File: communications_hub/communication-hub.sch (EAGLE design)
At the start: 47 parts, among them CON1 SM04B-GHS-TB, CON2 SM04B-GHS-TB, CON3 SM02B-GHS-TB, CON4 SM04B-GHS-TB, CON5 SM04B-GHS-TB, Q1 DMN5L06K, Q2 DMN5L06K, U1 TCAN1042HVDR, U2 TCAN1042HVDR

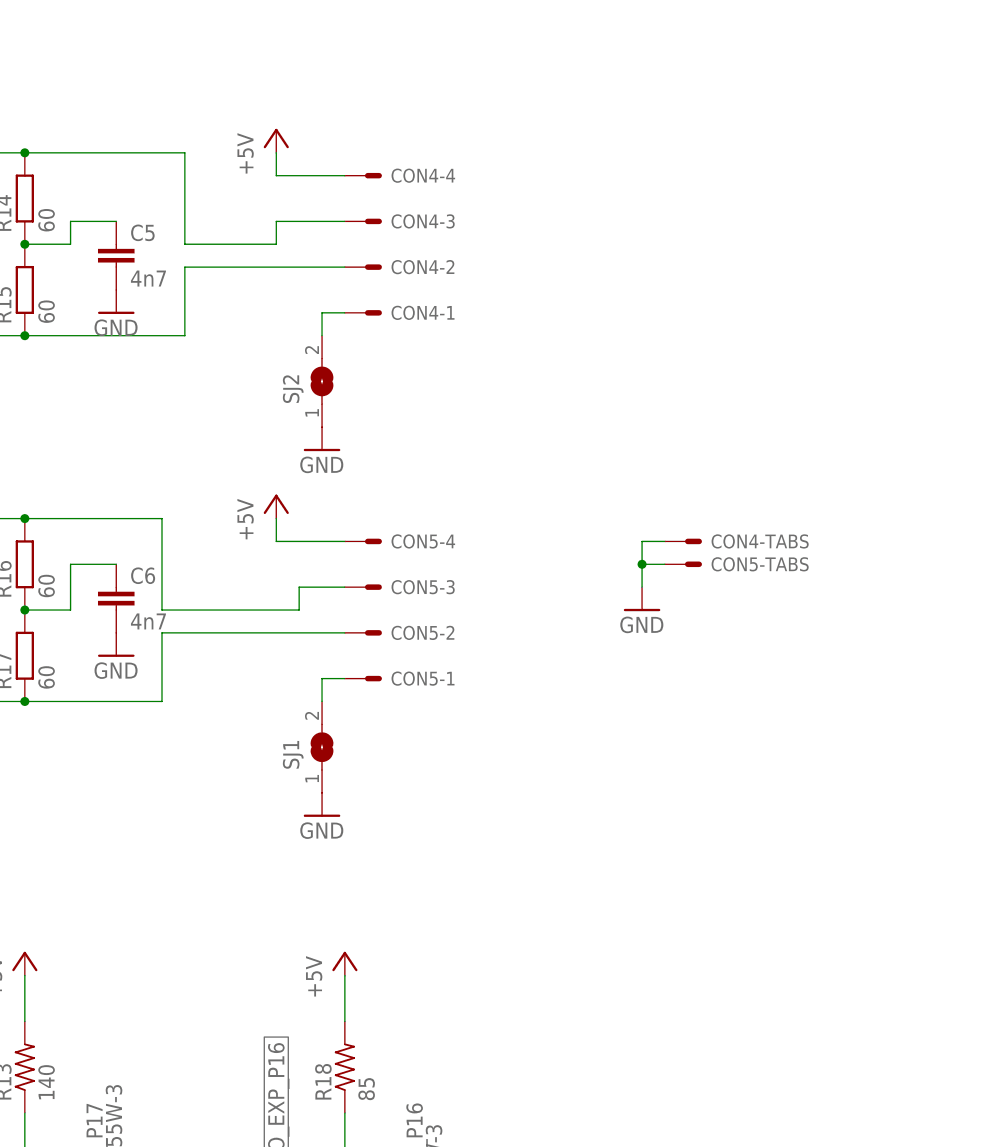
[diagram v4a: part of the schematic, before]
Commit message: Added TVS diodes. Needs some work.
Passes most DRC but has a few airwires.
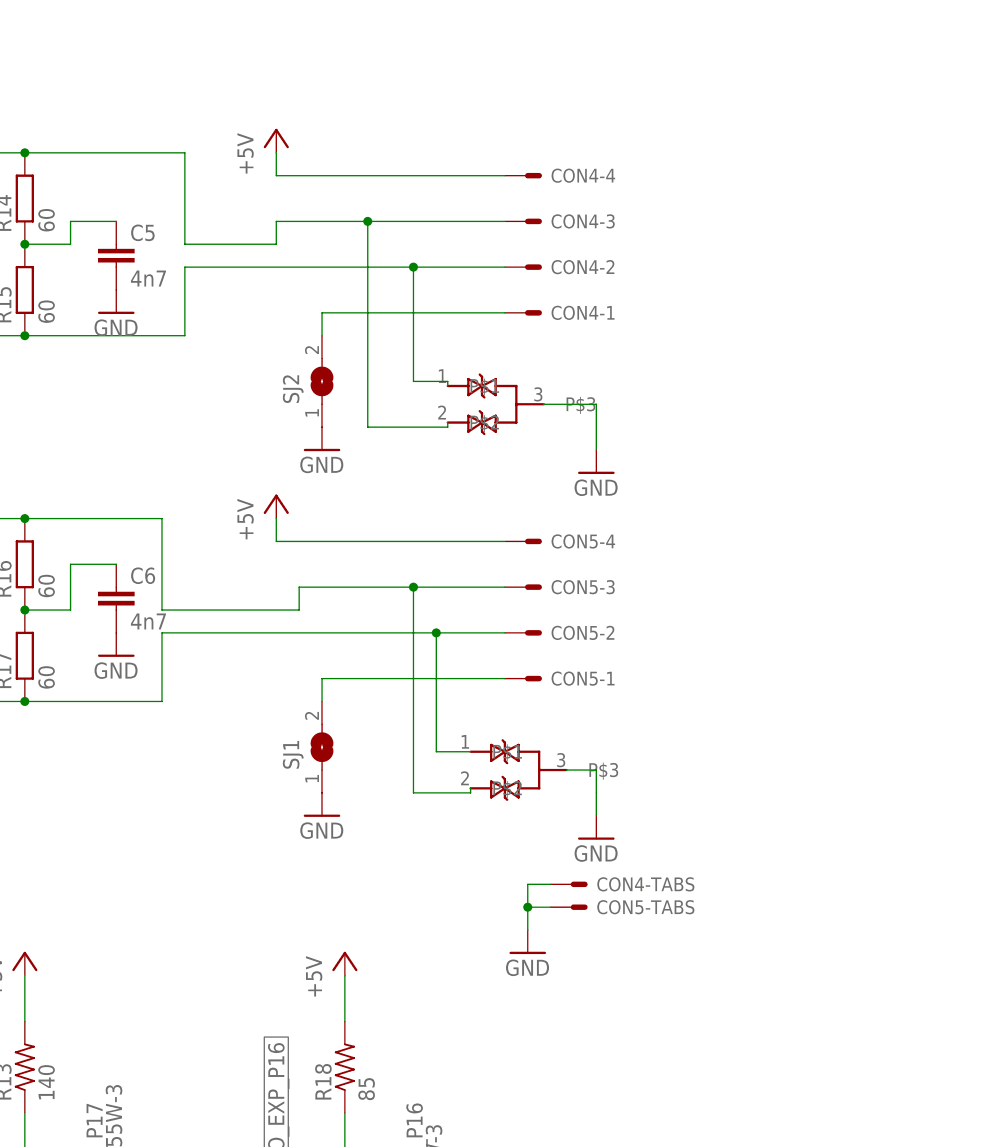
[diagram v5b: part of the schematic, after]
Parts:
- added U$4, U$5: NUP2105L, ARVP:NUP2105L
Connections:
- net GND: now also U$4.P$3, U$5.P$3
- net N$21: now also U$5.P$2
- net N$22: now also U$5.P$1
- net N$23: now also U$4.P$2
- net N$24: now also U$4.P$1
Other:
- moved on the sheet: CON4-1, CON4-2, CON4-3, CON4-4, CON4-TABS, CON5-1, CON5-2, CON5-3, CON5-4, CON5-TABS
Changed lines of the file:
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@@
 <?xml version="1.0" encoding="utf-8"?>
 <!DOCTYPE eagle SYSTEM "eagle.dtd">
-<eagle version="8.4.3">
+<eagle version="9.1.3">
 <drawing>
 <settings>
@@
 <part name="P+7" library="supply1" library_urn="urn:adsk.eagle:library:371" deviceset="+5V" device=""/>
 <part name="P+8" library="supply1" library_urn="urn:adsk.eagle:library:371" deviceset="+5V" device=""/>
+<part name="U$4" library="ARVP" deviceset="NUP2105L" device=""/>
+<part name="U$5" library="ARVP" deviceset="NUP2105L" device=""/>
+<part name="GND29" library="supply1" library_urn="urn:adsk.eagle:library:371" deviceset="GND" device=""/>
+<part name="GND30" library="supply1" library_urn="urn:adsk.eagle:library:371" deviceset="GND" device=""/>
 </parts>
 <sheets>
@@
 <instance part="GND10" gate="1" x="147.32" y="83.82"/>
 <instance part="GND25" gate="1" x="243.84" y="30.48"/>
-<instance part="GND28" gate="1" x="307.34" y="157.48"/>
+<instance part="GND28" gate="1" x="294.64" y="119.38"/>
 <instance part="FRAME1" gate="G$1" x="0" y="0"/>
 <instance part="FRAME1" gate="G$2" x="299.72" y="0"/>
-<instance part="CON4" gate="-1" x="274.32" y="190.5" rot="MR180"/>
-<instance part="CON4" gate="-2" x="274.32" y="195.58" rot="MR180"/>
-<instance part="CON4" gate="-3" x="274.32" y="200.66" rot="MR180"/>
-<instance part="CON4" gate="-TABS" x="309.88" y="165.1"/>
-<instance part="CON4" gate="-4" x="274.32" y="205.74" rot="MR180"/>
-<instance part="CON5" gate="-1" x="274.32" y="149.86" rot="MR180"/>
-<instance part="CON5" gate="-2" x="274.32" y="154.94" rot="MR180"/>
-<instance part="CON5" gate="-3" x="274.32" y="160.02" rot="MR180"/>
-<instance part="CON5" gate="-TABS" x="309.88" y="162.56"/>
-<instance part="CON5" gate="-4" x="274.32" y="165.1" rot="MR180"/>
+<instance part="CON4" gate="-1" x="292.1" y="190.5" rot="MR180"/>
+<instance part="CON4" gate="-2" x="292.1" y="195.58" rot="MR180"/>
+<instance part="CON4" gate="-3" x="292.1" y="200.66" rot="MR180"/>
+<instance part="CON4" gate="-TABS" x="297.18" y="127"/>
+<instance part="CON4" gate="-4" x="292.1" y="205.74" rot="MR180"/>
+<instance part="CON5" gate="-1" x="292.1" y="149.86" rot="MR180"/>
+<instance part="CON5" gate="-2" x="292.1" y="154.94" rot="MR180"/>
+<instance part="CON5" gate="-3" x="292.1" y="160.02" rot="MR180"/>
+<instance part="CON5" gate="-TABS" x="297.18" y="124.46"/>
+<instance part="CON5" gate="-4" x="292.1" y="165.1" rot="MR180"/>
 <instance part="P+5" gate="1" x="266.7" y="210.82"/>
 <instance part="P+6" gate="1" x="266.7" y="170.18"/>
@@
 <instance part="P+7" gate="1" x="238.76" y="119.38"/>
 <instance part="P+8" gate="1" x="274.32" y="119.38"/>
+<instance part="U$4" gate="G$1" x="289.56" y="180.34"/>
+<instance part="U$5" gate="G$1" x="292.1" y="139.7"/>
+<instance part="GND29" gate="1" x="302.26" y="132.08"/>
+<instance part="GND30" gate="1" x="302.26" y="172.72"/>
 </instances>
 <busses>
@@
 <segment>
 <pinref part="GND28" gate="1" pin="GND"/>
-<wire x1="307.34" y1="160.02" x2="307.34" y2="162.56" width="0.1524" layer="91"/>
-<wire x1="307.34" y1="162.56" x2="309.88" y2="162.56" width="0.1524" layer="91"/>
-<wire x1="307.34" y1="162.56" x2="307.34" y2="165.1" width="0.1524" layer="91"/>
-<wire x1="307.34" y1="165.1" x2="309.88" y2="165.1" width="0.1524" layer="91"/>
-<junction x="307.34" y="162.56"/>
+<wire x1="294.64" y1="121.92" x2="294.64" y2="124.46" width="0.1524" layer="91"/>
+<wire x1="294.64" y1="124.46" x2="297.18" y2="124.46" width="0.1524" layer="91"/>
+<wire x1="294.64" y1="124.46" x2="294.64" y2="127" width="0.1524" layer="91"/>
+<wire x1="294.64" y1="127" x2="297.18" y2="127" width="0.1524" layer="91"/>
+<junction x="294.64" y="124.46"/>
 <pinref part="CON4" gate="-TABS" pin="S"/>
 <pinref part="CON5" gate="-TABS" pin="S"/>
@@
 <pinref part="GND21" gate="1" pin="GND"/>
 <wire x1="243.84" y1="73.66" x2="243.84" y2="68.58" width="0.1524" layer="91"/>
+</segment>
+<segment>
+<pinref part="U$5" gate="G$1" pin="P$3"/>
+<wire x1="298.958" y1="139.7" x2="302.26" y2="139.7" width="0.1524" layer="91"/>
+<wire x1="302.26" y1="139.7" x2="302.26" y2="137.16" width="0.1524" layer="91"/>
+<wire x1="302.26" y1="134.62" x2="302.26" y2="137.16" width="0.1524" layer="91"/>
+<pinref part="GND29" gate="1" pin="GND"/>
+</segment>
+<segment>
+<pinref part="U$4" gate="G$1" pin="P$3"/>
+<wire x1="296.418" y1="180.34" x2="302.26" y2="180.34" width="0.1524" layer="91"/>
+<wire x1="302.26" y1="180.34" x2="302.26" y2="175.26" width="0.1524" layer="91"/>
+<pinref part="GND30" gate="1" pin="GND"/>
 </segment>
 </net>
@@
 <pinref part="P+5" gate="1" pin="+5V"/>
 <pinref part="CON4" gate="-4" pin="S"/>
-<wire x1="266.7" y1="205.74" x2="274.32" y2="205.74" width="0.1524" layer="91"/>
+<wire x1="266.7" y1="205.74" x2="292.1" y2="205.74" width="0.1524" layer="91"/>
 </segment>
 <segment>
@@
 <pinref part="P+6" gate="1" pin="+5V"/>
 <pinref part="CON5" gate="-4" pin="S"/>
-<wire x1="266.7" y1="165.1" x2="274.32" y2="165.1" width="0.1524" layer="91"/>
+<wire x1="266.7" y1="165.1" x2="292.1" y2="165.1" width="0.1524" layer="91"/>
 </segment>
 <segment>
@@
 <wire x1="269.24" y1="157.48" x2="269.24" y2="160.02" width="0.1524" layer="91"/>
 <pinref part="CON5" gate="-3" pin="S"/>
-<wire x1="269.24" y1="160.02" x2="274.32" y2="160.02" width="0.1524" layer="91"/>
+<wire x1="269.24" y1="160.02" x2="281.94" y2="160.02" width="0.1524" layer="91"/>
+<wire x1="281.94" y1="160.02" x2="292.1" y2="160.02" width="0.1524" layer="91"/>
+<wire x1="281.94" y1="160.02" x2="281.94" y2="137.16" width="0.1524" layer="91"/>
+<pinref part="U$5" gate="G$1" pin="P$2"/>
+<wire x1="281.94" y1="137.16" x2="288.29" y2="137.16" width="0.1524" layer="91"/>
+<wire x1="288.29" y1="137.16" x2="288.29" y2="137.668" width="0.1524" layer="91"/>
+<junction x="281.94" y="160.02"/>
 </segment>
 </net>
@@
 <junction x="238.76" y="147.32"/>
 <pinref part="CON5" gate="-2" pin="S"/>
-<wire x1="254" y1="154.94" x2="274.32" y2="154.94" width="0.1524" layer="91"/>
+<wire x1="254" y1="154.94" x2="284.48" y2="154.94" width="0.1524" layer="91"/>
+<pinref part="U$5" gate="G$1" pin="P$1"/>
+<wire x1="284.48" y1="154.94" x2="292.1" y2="154.94" width="0.1524" layer="91"/>
+<wire x1="284.48" y1="154.94" x2="284.48" y2="141.732" width="0.1524" layer="91"/>
+<junction x="284.48" y="154.94"/>
+<wire x1="284.48" y1="141.732" x2="288.29" y2="141.732" width="0.1524" layer="91"/>
 </segment>
 </net>
@@
 <junction x="238.76" y="208.28"/>
 <pinref part="CON4" gate="-3" pin="S"/>
-<wire x1="266.7" y1="200.66" x2="274.32" y2="200.66" width="0.1524" layer="91"/>
+<wire x1="266.7" y1="200.66" x2="276.86" y2="200.66" width="0.1524" layer="91"/>
+<wire x1="276.86" y1="200.66" x2="292.1" y2="200.66" width="0.1524" layer="91"/>
+<wire x1="276.86" y1="200.66" x2="276.86" y2="177.8" width="0.1524" layer="91"/>
+<junction x="276.86" y="200.66"/>
+<pinref part="U$4" gate="G$1" pin="P$2"/>
+<wire x1="276.86" y1="177.8" x2="285.75" y2="177.8" width="0.1524" layer="91"/>
+<wire x1="285.75" y1="177.8" x2="285.75" y2="178.308" width="0.1524" layer="91"/>
 </segment>
 </net>
@@
 <junction x="238.76" y="187.96"/>
 <pinref part="CON4" gate="-2" pin="S"/>
-<wire x1="256.54" y1="195.58" x2="274.32" y2="195.58" width="0.1524" layer="91"/>
+<wire x1="256.54" y1="195.58" x2="281.94" y2="195.58" width="0.1524" layer="91"/>
+<wire x1="281.94" y1="195.58" x2="292.1" y2="195.58" width="0.1524" layer="91"/>
+<wire x1="281.94" y1="195.58" x2="281.94" y2="182.88" width="0.1524" layer="91"/>
+<junction x="281.94" y="195.58"/>
+<pinref part="U$4" gate="G$1" pin="P$1"/>
+<wire x1="281.94" y1="182.88" x2="285.75" y2="182.88" width="0.1524" layer="91"/>
+<wire x1="285.75" y1="182.88" x2="285.75" y2="182.372" width="0.1524" layer="91"/>
 </segment>
 </net>
@@
 <wire x1="271.78" y1="149.86" x2="271.78" y2="147.32" width="0.1524" layer="91"/>
 <pinref part="CON5" gate="-1" pin="S"/>
-<wire x1="271.78" y1="149.86" x2="274.32" y2="149.86" width="0.1524" layer="91"/>
+<wire x1="271.78" y1="149.86" x2="292.1" y2="149.86" width="0.1524" layer="91"/>
 </segment>
 </net>
@@
 <wire x1="271.78" y1="190.5" x2="271.78" y2="187.96" width="0.1524" layer="91"/>
 <pinref part="CON4" gate="-1" pin="S"/>
-<wire x1="271.78" y1="190.5" x2="274.32" y2="190.5" width="0.1524" layer="91"/>
-</segment>
-</net>
+<wire x1="271.78" y1="190.5" x2="292.1" y2="190.5" width="0.1524" layer="91"/>
+</segment>
+</net>

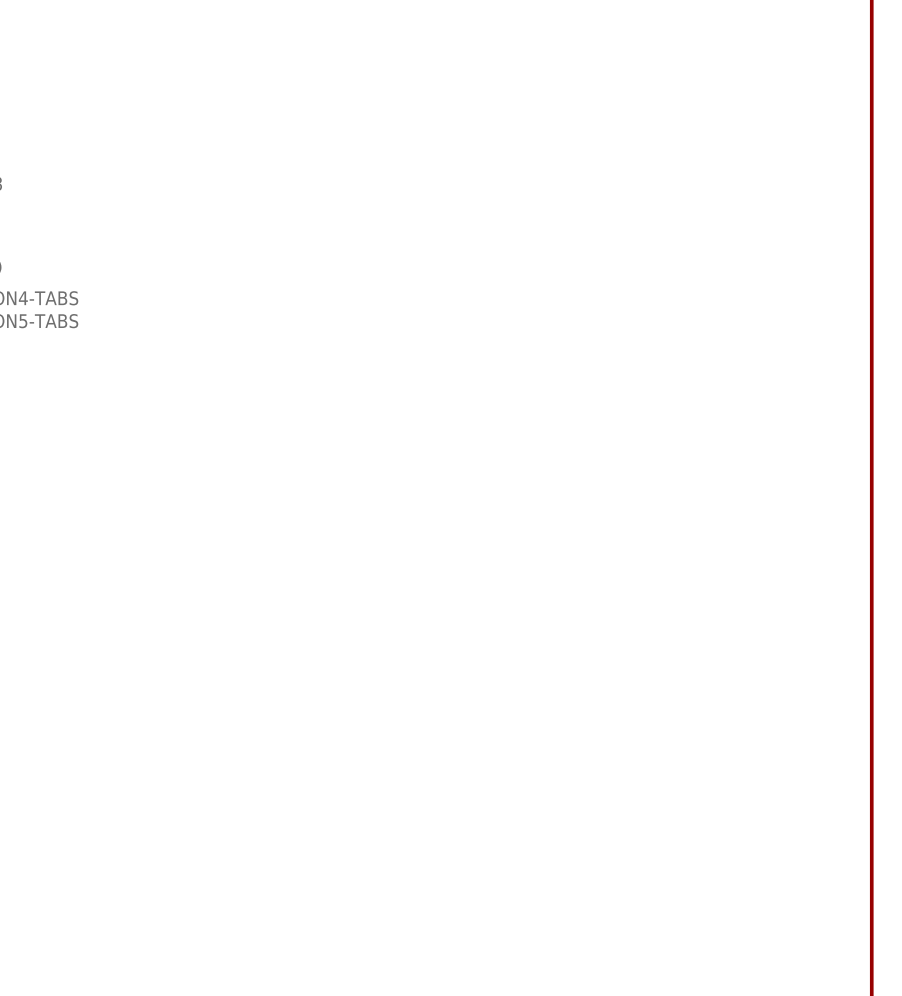
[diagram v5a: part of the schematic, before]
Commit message: Finally got around to finishing this.
Added test points and power bus indication LEDs.
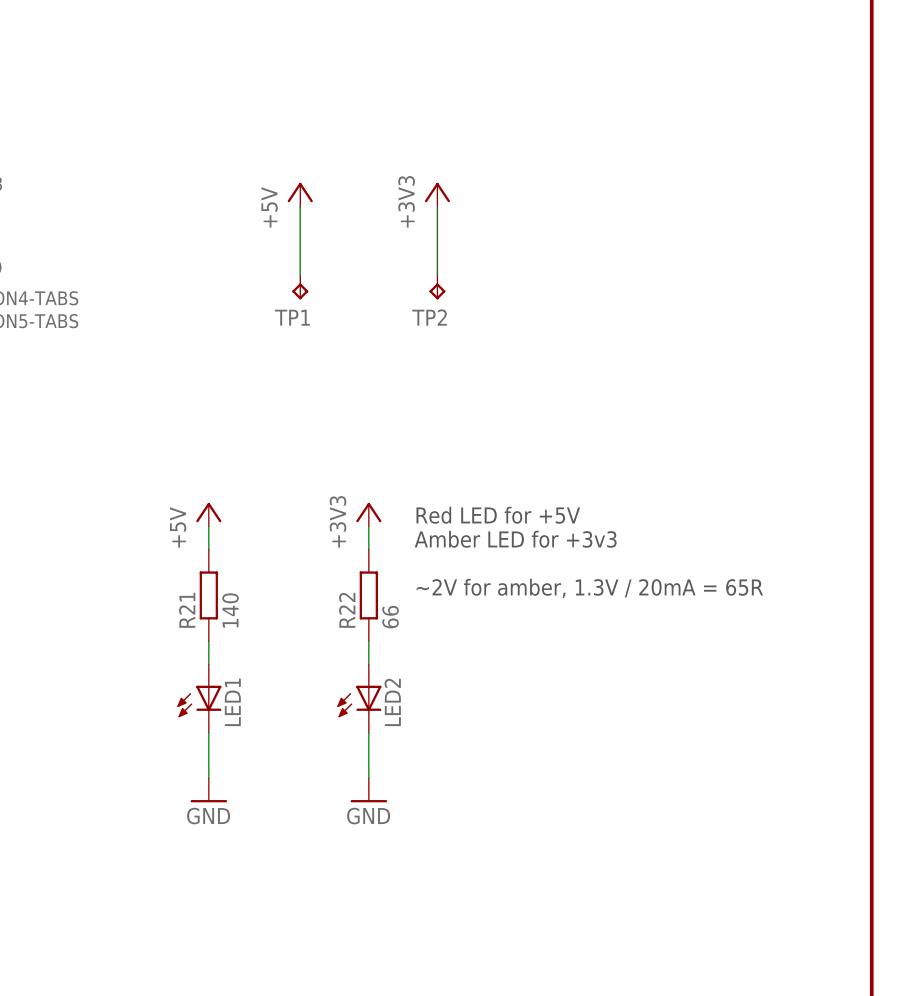
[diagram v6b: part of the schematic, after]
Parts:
- added LED1, LED2: (no value), led:LEDSMT1206
- added R21: 140, resistor:R-EU_R0805
- added R22: 66, resistor:R-EU_R0805
- added TP1, TP2: TPB2,54, testpad:TPB2,54
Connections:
- new net N$13: LED1.A, R21.1
- new net N$14: LED2.A, R22.1
- net +3V3: now also R22.2, TP2.TP
- net +5V: now also R21.2, TP1.TP
- net GND: now also LED1.C, LED2.C
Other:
- note added: "Red LED for +5V Amber LED for +3v3 ~2V for amber, 1.3V / 20mA = 65R"

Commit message: Added a reference ground test point.
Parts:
- added TP3: TPB2,54, testpad:TPB2,54
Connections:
- net GND: now also TP3.TP
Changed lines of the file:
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@@
 <part name="P+10" library="supply1" library_urn="urn:adsk.eagle:library:371" deviceset="+5V" device=""/>
 <part name="+3V2" library="supply1" library_urn="urn:adsk.eagle:library:371" deviceset="+3V3" device=""/>
+<part name="TP3" library="testpad" library_urn="urn:adsk.eagle:library:385" deviceset="TP" device="B2,54" package3d_urn="urn:adsk.eagle:package:27948/1"/>
+<part name="GND33" library="supply1" library_urn="urn:adsk.eagle:library:371" deviceset="GND" device=""/>
 </parts>
 <sheets>
@@
 <instance part="P+10" gate="1" x="337.82" y="139.7"/>
 <instance part="+3V2" gate="G$1" x="353.06" y="139.7"/>
+<instance part="TP3" gate="G$1" x="368.3" y="129.54"/>
+<instance part="GND33" gate="1" x="368.3" y="116.84"/>
 </instances>
 <busses>
@@
 <wire x1="345.44" y1="78.74" x2="345.44" y2="73.66" width="0.1524" layer="91"/>
 </segment>
+<segment>
+<pinref part="TP3" gate="G$1" pin="TP"/>
+<wire x1="368.3" y1="127" x2="368.3" y2="119.38" width="0.1524" layer="91"/>
+<pinref part="GND33" gate="1" pin="GND"/>
+</segment>
 </net>
